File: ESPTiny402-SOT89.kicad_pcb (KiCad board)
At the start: 2 copper layers, 26.4 x 23.9 mm, 20 parts, among them J1 Conn_01x10_Male, J2 Conn_01x10_Male, J3 Conn_01x04_Male, U1 ESP-01v090, U2 ATtiny402-SS, U3 MCP1700

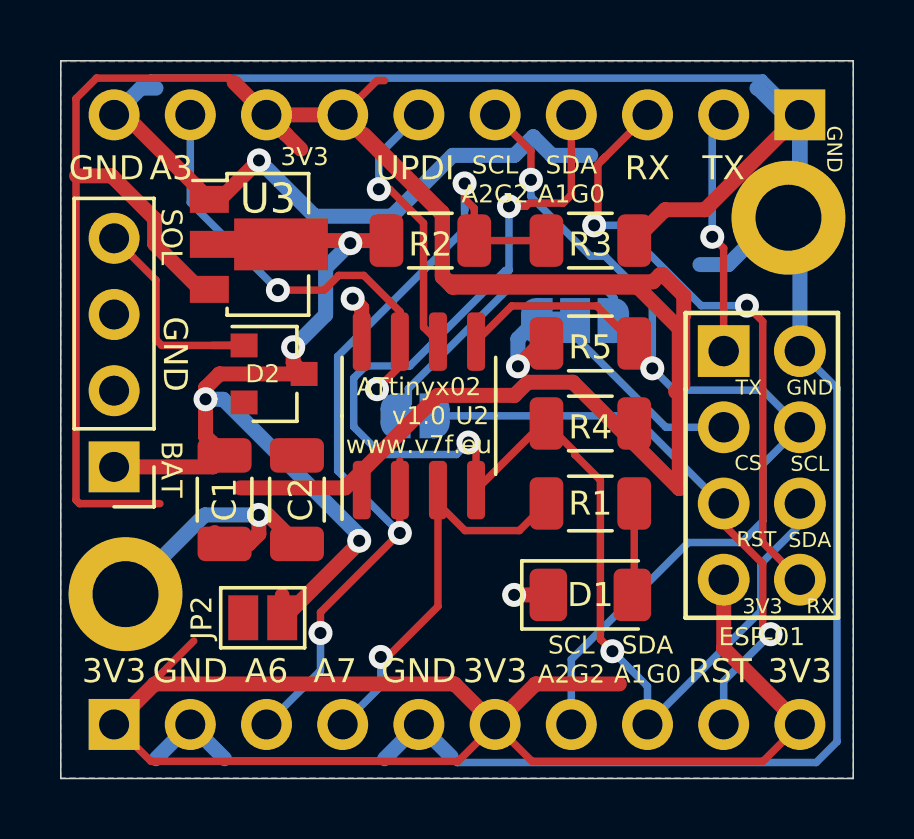
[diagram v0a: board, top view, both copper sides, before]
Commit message: SOT89 version reorder
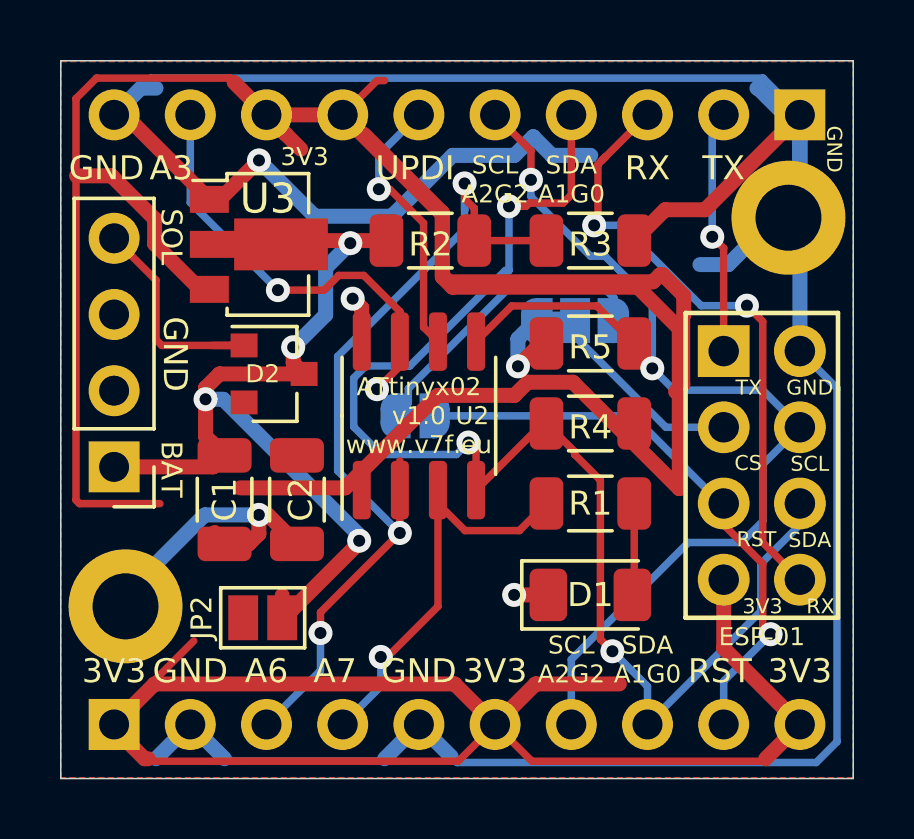
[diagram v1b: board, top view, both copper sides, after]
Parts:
- moved REF** 0.41 mm to (47.9, 58.5)
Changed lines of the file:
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@@
     (thickness 1.6)
     (drawings 55)
-    (tracks 308)
+    (tracks 312)
     (zones 0)
     (modules 20)
@@
   )
   (module MountingHole:MountingHole_2.2mm_M2_DIN965_Pad (layer F.Cu)
-    (at 47.879 58.1406)
+    (at 47.879 58.547)
     (descr "Mounting Hole 2.2mm, M2, DIN965")
     (tags "mounting hole 2.2mm m2 din965")
@@
   (segment (start 61.423001 63.709001) (end 60.198 62.484) (width 0.25) (layer F.Cu) (net 2) (status 20))
   (segment (start 69.132999 63.709001) (end 61.423001 63.709001) (width 0.25) (layer F.Cu) (net 2))
-  (segment (start 70.358 62.484) (end 69.132999 63.709001) (width 0.25) (layer F.Cu) (net 2) (status 10))
-  (segment (start 48.723001 63.709001) (end 47.498 62.484) (width 0.25) (layer F.Cu) (net 2) (status 20))
   (segment (start 58.972999 63.709001) (end 48.723001 63.709001) (width 0.25) (layer F.Cu) (net 2))
   (segment (start 60.198 62.484) (end 58.972999 63.709001) (width 0.25) (layer F.Cu) (net 2) (status 10))
@@
   (segment (start 52.578 42.164) (end 51.4985 41.0845) (width 0.5) (layer F.Cu) (net 2) (status 10))
   (segment (start 51.352999 40.938999) (end 51.4985 41.0845) (width 0.25) (layer F.Cu) (net 2))
+  (segment (start 47.498 62.611) (end 48.514 63.627) (width 0.5) (layer F.Cu) (net 2) (status 10))
+  (segment (start 47.498 62.484) (end 47.498 62.611) (width 0.5) (layer F.Cu) (net 2) (status 30))
+  (segment (start 48.723001 63.709001) (end 48.641 63.627) (width 0.25) (layer F.Cu) (net 2))
+  (segment (start 48.514 63.627) (end 48.641 63.627) (width 0.5) (layer F.Cu) (net 2))
+  (segment (start 70.358 62.484) (end 69.215 63.627) (width 0.5) (layer F.Cu) (net 2) (status 10))
+  (segment (start 69.215 63.627) (end 69.132999 63.709001) (width 0.25) (layer F.Cu) (net 2))
   (segment (start 64.8355 58.1035) (end 64.773 58.166) (width 0.25) (layer F.Cu) (net 4) (status 30))
   (segment (start 64.8355 55.118) (end 64.8355 58.1035) (width 0.25) (layer F.Cu) (net 4) (status 30))

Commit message: SOT89 add TH position
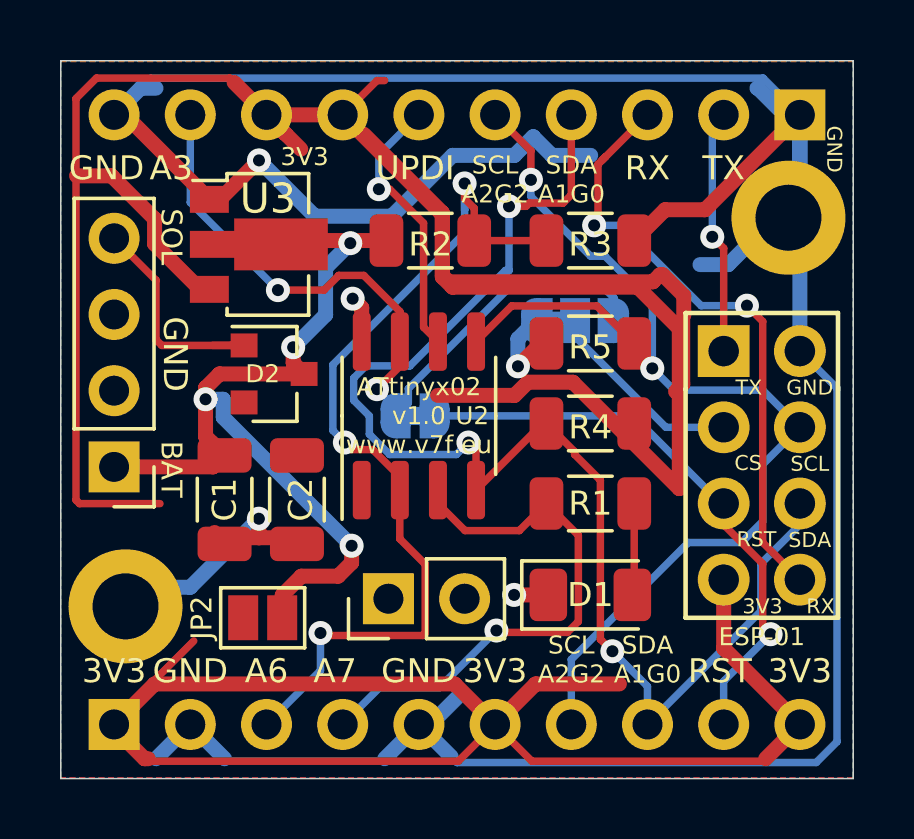
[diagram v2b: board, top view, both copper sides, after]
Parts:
- added REF**: PinHeader_1x02_P2.54mm_Vertical, Connector_PinHeader_2.54mm:PinHeader_1x02_P2.54mm_Vertical, F.Cu at (56.6, 58.3)
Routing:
- net +3V3: track 149.3 -> 141.5 mm
- net /A7: track 14.1 -> 18.8 mm
- net GND: track 122.9 -> 124.3 mm
